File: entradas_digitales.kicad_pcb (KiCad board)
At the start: 2 copper layers, 100 x 50 mm, 68 parts, among them J1 Opto5-8, J2 Opto1-4, J3 Entrada, J4 Salida, U1 TLP627-4, U2 TLP627-4, U3 4021

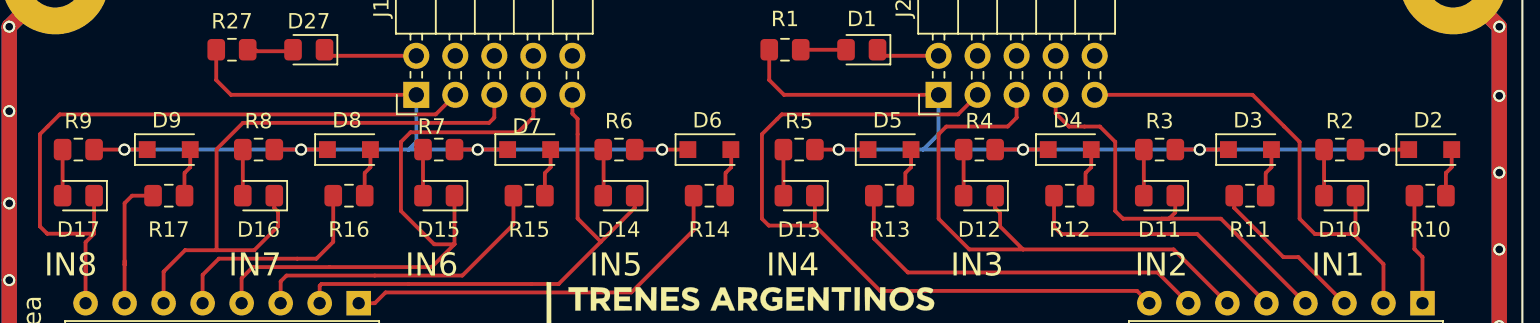
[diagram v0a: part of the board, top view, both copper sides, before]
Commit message: Agregado de BOM
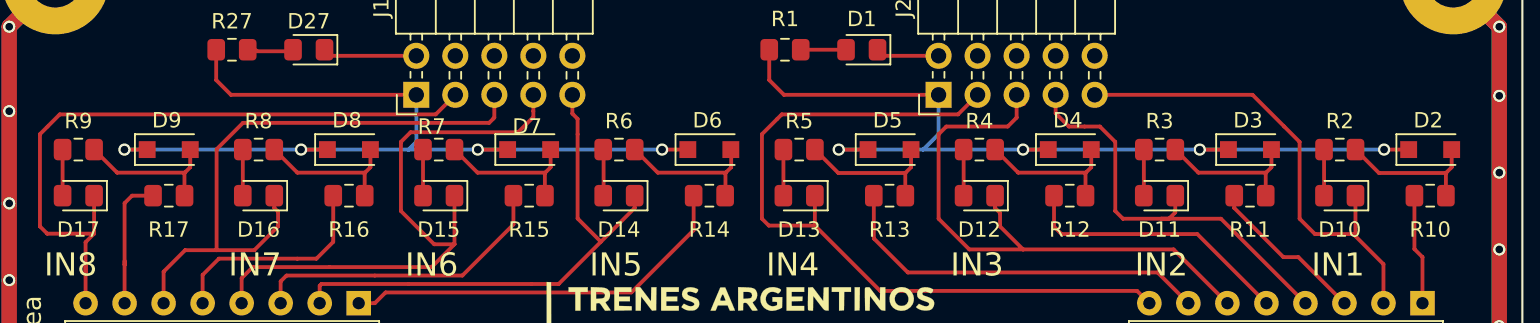
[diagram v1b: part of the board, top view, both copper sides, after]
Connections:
- R2 pad 1: /24V-A -> Net-(D2-Pad2)
- R3 pad 1: /24V-A -> Net-(D3-Pad2)
- R4 pad 1: /24V-A -> Net-(D4-Pad2)
- R5 pad 1: /24V-A -> Net-(D5-Pad2)
- R6 pad 1: /24V-B -> Net-(D6-Pad2)
- R7 pad 1: /24V-B -> Net-(D7-Pad2)
- R8 pad 1: /24V-B -> Net-(D8-Pad2)
- R9 pad 1: /24V-B -> Net-(D9-Pad2)
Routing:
- net /24V-B: track 68.0 -> 61.0 mm
- net /24V-A: track 66.7 -> 59.9 mm
- net Net-(D6-Pad2): track 3.12 -> 9.67 mm
- net Net-(D7-Pad2): track 3.12 -> 9.65 mm
- net Net-(D9-Pad2): track 3.12 -> 9.65 mm
- net Net-(D8-Pad2): track 3.12 -> 9.65 mm
- net Net-(D3-Pad2): track 3.12 -> 9.65 mm
- net Net-(D4-Pad2): track 3.12 -> 9.65 mm
- net Net-(D2-Pad2): track 3.69 -> 10.2 mm
- net Net-(D5-Pad2): track 3.12 -> 9.63 mm
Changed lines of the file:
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@@
     (thickness 1.6)
     (drawings 51)
-    (tracks 658)
+    (tracks 666)
     (zones 0)
     (modules 68)
@@
     )
     (pad 1 smd roundrect (at -1.025 0 180) (size 1.15 1.4) (layers F.Cu F.Paste F.Mask) (roundrect_rratio 0.217391)
-      (net 50 /24V-B))
+      (net 23 "Net-(D9-Pad2)"))
     (pad 2 smd roundrect (at 1.025 0 180) (size 1.15 1.4) (layers F.Cu F.Paste F.Mask) (roundrect_rratio 0.217391)
       (net 14 "Net-(D17-Pad2)"))
@@
       (net 13 "Net-(D16-Pad2)"))
     (pad 1 smd roundrect (at -1.025 0 180) (size 1.15 1.4) (layers F.Cu F.Paste F.Mask) (roundrect_rratio 0.217391)
-      (net 50 /24V-B))
+      (net 22 "Net-(D8-Pad2)"))
     (model ${KISYS3DMOD}/Resistor_SMD.3dshapes/R_0805_2012Metric.wrl
       (at (xyz 0 0 0))
@@
     )
     (pad 1 smd roundrect (at -1.025 0 180) (size 1.15 1.4) (layers F.Cu F.Paste F.Mask) (roundrect_rratio 0.217391)
-      (net 50 /24V-B))
+      (net 19 "Net-(D7-Pad2)"))
     (pad 2 smd roundrect (at 1.025 0 180) (size 1.15 1.4) (layers F.Cu F.Paste F.Mask) (roundrect_rratio 0.217391)
       (net 12 "Net-(D15-Pad2)"))
@@
       (net 11 "Net-(D14-Pad2)"))
     (pad 1 smd roundrect (at -1.025 0 180) (size 1.15 1.4) (layers F.Cu F.Paste F.Mask) (roundrect_rratio 0.217391)
-      (net 50 /24V-B))
+      (net 4 "Net-(D6-Pad2)"))
     (model ${KISYS3DMOD}/Resistor_SMD.3dshapes/R_0805_2012Metric.wrl
       (at (xyz 0 0 0))
@@
     )
     (pad 1 smd roundrect (at -1.025 0 180) (size 1.15 1.4) (layers F.Cu F.Paste F.Mask) (roundrect_rratio 0.217391)
-      (net 52 /24V-A))
+      (net 34 "Net-(D5-Pad2)"))
     (pad 2 smd roundrect (at 1.025 0 180) (size 1.15 1.4) (layers F.Cu F.Paste F.Mask) (roundrect_rratio 0.217391)
       (net 10 "Net-(D13-Pad2)"))
@@
       (net 9 "Net-(D12-Pad2)"))
     (pad 1 smd roundrect (at -1.025 0 180) (size 1.15 1.4) (layers F.Cu F.Paste F.Mask) (roundrect_rratio 0.217391)
-      (net 52 /24V-A))
+      (net 3 "Net-(D4-Pad2)"))
     (model ${KISYS3DMOD}/Resistor_SMD.3dshapes/R_0805_2012Metric.wrl
       (at (xyz 0 0 0))
@@
     )
     (pad 1 smd roundrect (at -1.025 0 180) (size 1.15 1.4) (layers F.Cu F.Paste F.Mask) (roundrect_rratio 0.217391)
-      (net 52 /24V-A))
+      (net 18 "Net-(D3-Pad2)"))
     (pad 2 smd roundrect (at 1.025 0 180) (size 1.15 1.4) (layers F.Cu F.Paste F.Mask) (roundrect_rratio 0.217391)
       (net 6 "Net-(D11-Pad2)"))
@@
       (net 7 "Net-(D10-Pad2)"))
     (pad 1 smd roundrect (at -1.025 0 180) (size 1.15 1.4) (layers F.Cu F.Paste F.Mask) (roundrect_rratio 0.217391)
-      (net 52 /24V-A))
+      (net 15 "Net-(D2-Pad2)"))
     (model ${KISYS3DMOD}/Resistor_SMD.3dshapes/R_0805_2012Metric.wrl
       (at (xyz 0 0 0))
@@
   (segment (start 179.938 84.15) (end 179.588 84.5) (width 0.25) (layer F.Cu) (net 3))
   (segment (start 179.938 83) (end 179.938 84.15) (width 0.25) (layer F.Cu) (net 3))
+  (segment (start 175.18 84.5) (end 173.68 83) (width 0.25) (layer F.Cu) (net 3))
+  (segment (start 179.588 84.5) (end 175.18 84.5) (width 0.25) (layer F.Cu) (net 3))
   (segment (start 156.125 86) (end 156.125 84.525) (width 0.25) (layer F.Cu) (net 4))
   (segment (start 156.5 84.15) (end 156.15 84.5) (width 0.25) (layer F.Cu) (net 4))
   (segment (start 156.5 83) (end 156.5 84.15) (width 0.25) (layer F.Cu) (net 4))
+  (segment (start 151.718 84.5) (end 150.218 83) (width 0.25) (layer F.Cu) (net 4))
+  (segment (start 156.15 84.5) (end 151.718 84.5) (width 0.25) (layer F.Cu) (net 4))
   (segment (start 133.3 93) (end 133.99994 92.30006) (width 0.25) (layer F.Cu) (net 5))
   (segment (start 132.25 93) (end 133.3 93) (width 0.25) (layer F.Cu) (net 5))
@@
   (segment (start 203.4 83) (end 203.4 84.15) (width 0.25) (layer F.Cu) (net 15))
   (segment (start 203.025 84.525) (end 203.05 84.5) (width 0.25) (layer F.Cu) (net 15))
+  (segment (start 198.667 84.525) (end 197.142 83) (width 0.25) (layer F.Cu) (net 15))
+  (segment (start 203.025 84.525) (end 198.667 84.525) (width 0.25) (layer F.Cu) (net 15))
   (segment (start 200.975 86) (end 200.975 89.475) (width 0.25) (layer F.Cu) (net 16))
   (segment (start 201.5 90) (end 201.5 93) (width 0.25) (layer F.Cu) (net 16))
@@
   (segment (start 191.669 84.15) (end 191.319 84.5) (width 0.25) (layer F.Cu) (net 18))
   (segment (start 191.669 83) (end 191.669 84.15) (width 0.25) (layer F.Cu) (net 18))
+  (segment (start 186.911 84.5) (end 185.411 83) (width 0.25) (layer F.Cu) (net 18))
+  (segment (start 191.319 84.5) (end 186.911 84.5) (width 0.25) (layer F.Cu) (net 18))
   (segment (start 144.37 86) (end 144.37 84.525) (width 0.25) (layer F.Cu) (net 19))
   (segment (start 144.745 84.15) (end 144.395 84.5) (width 0.25) (layer F.Cu) (net 19))
   (segment (start 144.745 83) (end 144.745 84.15) (width 0.25) (layer F.Cu) (net 19))
+  (segment (start 139.987 84.5) (end 138.487 83) (width 0.25) (layer F.Cu) (net 19))
+  (segment (start 144.395 84.5) (end 139.987 84.5) (width 0.25) (layer F.Cu) (net 19))
   (segment (start 133.29996 91.20004) (end 127.54996 91.20004) (width 0.25) (layer F.Cu) (net 20))
   (segment (start 127.17 91.58) (end 127.17 93) (width 0.25) (layer F.Cu) (net 20))
@@
   (segment (start 133.014 84.15) (end 132.664 84.5) (width 0.25) (layer F.Cu) (net 22))
   (segment (start 133.014 83) (end 133.014 84.15) (width 0.25) (layer F.Cu) (net 22))
+  (segment (start 128.256 84.5) (end 126.756 83) (width 0.25) (layer F.Cu) (net 22))
+  (segment (start 132.664 84.5) (end 128.256 84.5) (width 0.25) (layer F.Cu) (net 22))
   (segment (start 120.908 86) (end 120.908 84.525) (width 0.25) (layer F.Cu) (net 23))
-  (segment (start 121.283 84.15) (end 120.933 84.5) (width 0.25) (layer F.Cu) (net 23))
   (segment (start 121.283 83) (end 121.283 84.15) (width 0.25) (layer F.Cu) (net 23))
+  (segment (start 121.283 84.15) (end 120.933 84.5) (width 0.25) (layer F.Cu) (net 23))
+  (segment (start 116.525 84.5) (end 115.025 83) (width 0.25) (layer F.Cu) (net 23))
+  (segment (start 120.933 84.5) (end 116.525 84.5) (width 0.25) (layer F.Cu) (net 23))
   (segment (start 118.862676 86) (end 117.5 86) (width 0.25) (layer F.Cu) (net 24))
   (segment (start 117.01 86.49) (end 117.01 90.5) (width 0.25) (layer F.Cu) (net 24))
@@
   (segment (start 168.207 84.15) (end 167.857 84.5) (width 0.25) (layer F.Cu) (net 34))
   (segment (start 168.207 83) (end 168.207 84.15) (width 0.25) (layer F.Cu) (net 34))
+  (segment (start 163.474 84.525) (end 161.949 83) (width 0.25) (layer F.Cu) (net 34))
+  (segment (start 167.832 84.525) (end 163.474 84.525) (width 0.25) (layer F.Cu) (net 34))
   (segment (start 184.26 91) (end 186.26 93) (width 0.25) (layer F.Cu) (net 35))
   (segment (start 168 91) (end 184.26 91) (width 0.25) (layer F.Cu) (net 35))
@@
   (segment (start 153.7 83) (end 152.9 83) (width 0.25) (layer F.Cu) (net 50))
   (segment (start 152.9 83) (end 152 83) (width 0.25) (layer F.Cu) (net 50))
-  (segment (start 117 83) (end 115.025 83) (width 0.25) (layer F.Cu) (net 50))
   (via (at 117 83) (size 0.8) (drill 0.5) (layers F.Cu B.Cu) (net 50))
-  (segment (start 128.5 83) (end 126.756 83) (width 0.25) (layer F.Cu) (net 50))
   (via (at 128.5 83) (size 0.8) (drill 0.5) (layers F.Cu B.Cu) (net 50))
-  (segment (start 140 83) (end 138.487 83) (width 0.25) (layer F.Cu) (net 50))
   (via (at 140 83) (size 0.8) (drill 0.5) (layers F.Cu B.Cu) (net 50))
-  (segment (start 152 83) (end 150.242 83) (width 0.25) (layer F.Cu) (net 50))
   (via (at 152 83) (size 0.8) (drill 0.5) (layers F.Cu B.Cu) (net 50))
   (segment (start 152 83) (end 140 83) (width 0.25) (layer B.Cu) (net 50))
@@
   (segment (start 199.8 83) (end 199 83) (width 0.25) (layer F.Cu) (net 52))
   (segment (start 200.6 83) (end 199.8 83) (width 0.25) (layer F.Cu) (net 52))
-  (segment (start 163.5 83) (end 161.949 83) (width 0.25) (layer F.Cu) (net 52))
   (via (at 163.5 83) (size 0.8) (drill 0.5) (layers F.Cu B.Cu) (net 52))
-  (segment (start 175.5 83) (end 173.68 83) (width 0.25) (layer F.Cu) (net 52))
   (via (at 175.5 83) (size 0.8) (drill 0.5) (layers F.Cu B.Cu) (net 52))
-  (segment (start 187 83) (end 185.411 83) (width 0.25) (layer F.Cu) (net 52))
   (via (at 187 83) (size 0.8) (drill 0.5) (layers F.Cu B.Cu) (net 52))
-  (segment (start 199 83) (end 197.142 83) (width 0.25) (layer F.Cu) (net 52))
   (via (at 199 83) (size 0.8) (drill 0.5) (layers F.Cu B.Cu) (net 52))
   (segment (start 199 83) (end 187 83) (width 0.25) (layer B.Cu) (net 52))
